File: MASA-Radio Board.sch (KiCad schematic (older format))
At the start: 35 parts, among them IC1 FAN4010IL6X_F113, IC2 FAN4010IL6X_F113, J1 SC_19-20, J2 Conn_01x03_Male, J3 Conn_01x02, J4 Conn_01x06, J5 Conn_01x06, J6 Conn_01x02, J7 UJ2-MBH-1-SMT-TR, U1 MP5077GG-Z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

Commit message: Modified CAN from 5.0V to 3.3V
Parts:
- renumbered R5 to R6, R6 to R7, R7 to R8, R8 to R9, U5 to U6
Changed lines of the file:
@@
 XBee
 $Sheet
-S 8050 6700 1150 2800
+S 8200 6700 1150 2800
 U 5E22EDDC
 F0 "CAN_Template" 50
 F1 "CAN_Template.sch" 50
-F2 "CAN_L" I L 8050 6850 50
-F3 "CAN_H" I L 8050 7050 50
-F4 "SI" I L 8050 7250 50
-F5 "SO" I L 8050 7450 50
-F6 "CS" I L 8050 7650 50
-F7 "SCK" I L 8050 7850 50
-F8 "INT" I L 8050 8100 50
-F9 "RX0BF" I L 8050 8300 50
-F10 "RX1BF" I L 8050 8500 50
-F11 "TX0RTS" I L 8050 8700 50
-F12 "TX1RTS" I L 8050 8950 50
-F13 "TX2RTS" I L 8050 9150 50
-F14 "RESET" I L 8050 9400 50
+F2 "CAN_L" I L 8200 6850 50
+F3 "CAN_H" I L 8200 7050 50
+F4 "SI" I L 8200 7250 50
+F5 "SO" I L 8200 7450 50
+F6 "CS" I L 8200 7650 50
+F7 "SCK" I L 8200 7850 50
+F8 "INT" I L 8200 8100 50
+F9 "RX0BF" I L 8200 8300 50
+F10 "RX1BF" I L 8200 8500 50
+F11 "TX0RTS" I L 8200 8700 50
+F12 "TX1RTS" I L 8200 8950 50
+F13 "TX2RTS" I L 8200 9150 50
+F14 "RESET" I L 8200 9400 50
 $EndSheet
-Text Notes 7850 10000 0    157  ~ 0
+Text Notes 7850 9950 0    157  ~ 0
 CAN_Template
-Text Notes 11450 5850 0    157  ~ 0
+Text Notes 11300 5850 0    157  ~ 0
 BL654PA MCU
 Wire Wire Line
@@
 	0    -1   -1   0
 $EndComp
-Text GLabel 8050 6850 0    50   Input ~ 0
+Text GLabel 8200 6850 0    50   Input ~ 0
 CAN_L
-Text GLabel 8050 7050 0    50   Input ~ 0
+Text GLabel 8200 7050 0    50   Input ~ 0
 CAN_H
-Text GLabel 8050 8100 0    50   Input ~ 0
+Text GLabel 8200 8100 0    50   Input ~ 0
 CAN_INT
-Text GLabel 8050 7650 0    50   Input ~ 0
+Text GLabel 8200 7650 0    50   Input ~ 0
 CS
-Text GLabel 8050 7850 0    50   Input ~ 0
+Text GLabel 8200 7850 0    50   Input ~ 0
 SPI_CLK
-Text GLabel 8050 9400 0    50   Input ~ 0
+Text GLabel 8200 9400 0    50   Input ~ 0
 CAN_RST
-Text GLabel 8050 9150 0    50   Input ~ 0
+Text GLabel 8200 9150 0    50   Input ~ 0
 TX2RTS
-Text GLabel 8050 8950 0    50   Input ~ 0
+Text GLabel 8200 8950 0    50   Input ~ 0
 TX1RTS
-Text GLabel 8050 8700 0    50   Input ~ 0
+Text GLabel 8200 8700 0    50   Input ~ 0
 TX0RTS
-Text GLabel 8050 8500 0    50   Input ~ 0
+Text GLabel 8200 8500 0    50   Input ~ 0
 RX1BF
-Text GLabel 8050 8300 0    50   Input ~ 0
+Text GLabel 8200 8300 0    50   Input ~ 0
 RX0BF
 Text GLabel 10450 3950 0    50   Input ~ 0
@@
 Text GLabel 10450 4050 0    50   Input ~ 0
 SPI_MOSI
-Text GLabel 8050 7450 0    50   Input ~ 0
+Text GLabel 8200 7450 0    50   Input ~ 0
 SPI_MISO
-Text GLabel 8050 7250 0    50   Input ~ 0
+Text GLabel 8200 7250 0    50   Input ~ 0
 SPI_MOSI
 Text GLabel 10450 4250 0    50   Input ~ 0
@@
 Current Sense IC
 $Comp
-L MASA_Library:MP5077GG-Z U5
+L MASA_Library:MP5077GG-Z U6
 U 1 1 5E25F7C2
 P 3700 11750
-F 0 "U5" H 3700 12165 50  0000 C CNN
+F 0 "U6" H 3700 12165 50  0000 C CNN
 F 1 "MP5077GG-Z" H 3700 12074 50  0000 C CNN
 F 2 "MASA_Library:MP5077GG-Z" H 3700 11650 50  0001 C CNN
@@
 $EndComp
 $Comp
-L Device:R_Small_US R5
+L Device:R_Small_US R6
 U 1 1 5E278AC5
 P 4350 12000
-F 0 "R5" V 4145 12000 50  0000 C CNN
+F 0 "R6" V 4145 12000 50  0000 C CNN
 F 1 "820k" V 4236 12000 50  0000 C CNN
 F 2 "" H 4350 12000 50  0001 C CNN
@@
 	5050 11900 5050 11950
 $Comp
-L Device:R_US R6
+L Device:R_US R7
 U 1 1 5E285E1D
 P 5350 11950
-F 0 "R6" V 5280 12068 50  0000 C CNN
+F 0 "R7" V 5280 12068 50  0000 C CNN
 F 1 "1" V 5267 11832 50  0000 C CNN
 F 2 "" V 5390 11940 50  0001 C CNN
@@
 Connection ~ 4700 11600
 $Comp
-L Device:R_Small_US R7
+L Device:R_Small_US R8
 U 1 1 5E28C88E
 P 6300 11950
-F 0 "R7" H 6368 11996 50  0000 L CNN
+F 0 "R8" H 6368 11996 50  0000 L CNN
 F 1 "1" H 6368 11905 50  0000 L CNN
 F 2 "" H 6300 11950 50  0001 C CNN
@@
 $EndComp
 $Comp
-L Device:R_Small_US R8
+L Device:R_Small_US R9
 U 1 1 5E298170
 P 6850 11950
-F 0 "R8" H 6918 11996 50  0000 L CNN
+F 0 "R9" H 6918 11996 50  0000 L CNN
 F 1 "3k" H 6918 11905 50  0000 L CNN
 F 2 "" H 6850 11950 50  0001 C CNN

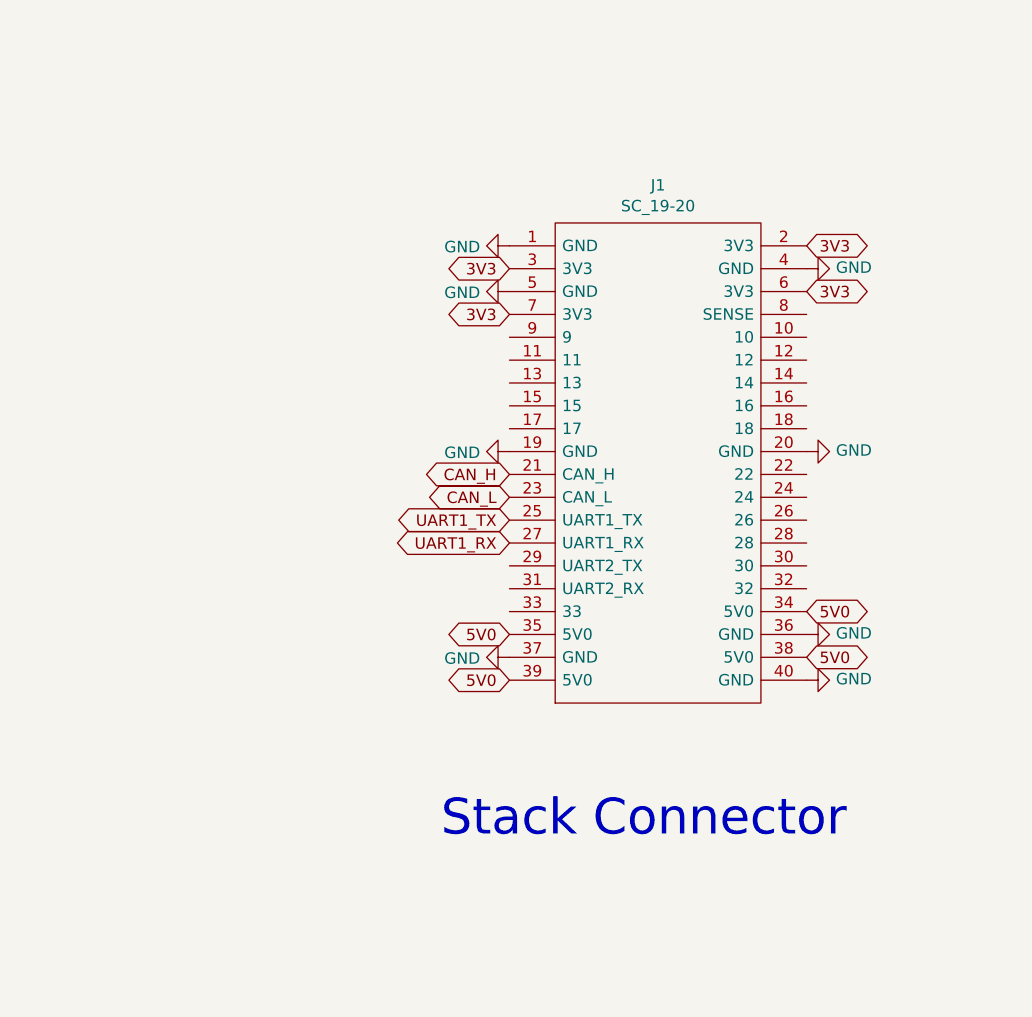
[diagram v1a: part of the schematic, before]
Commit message: Connected stack to xbee
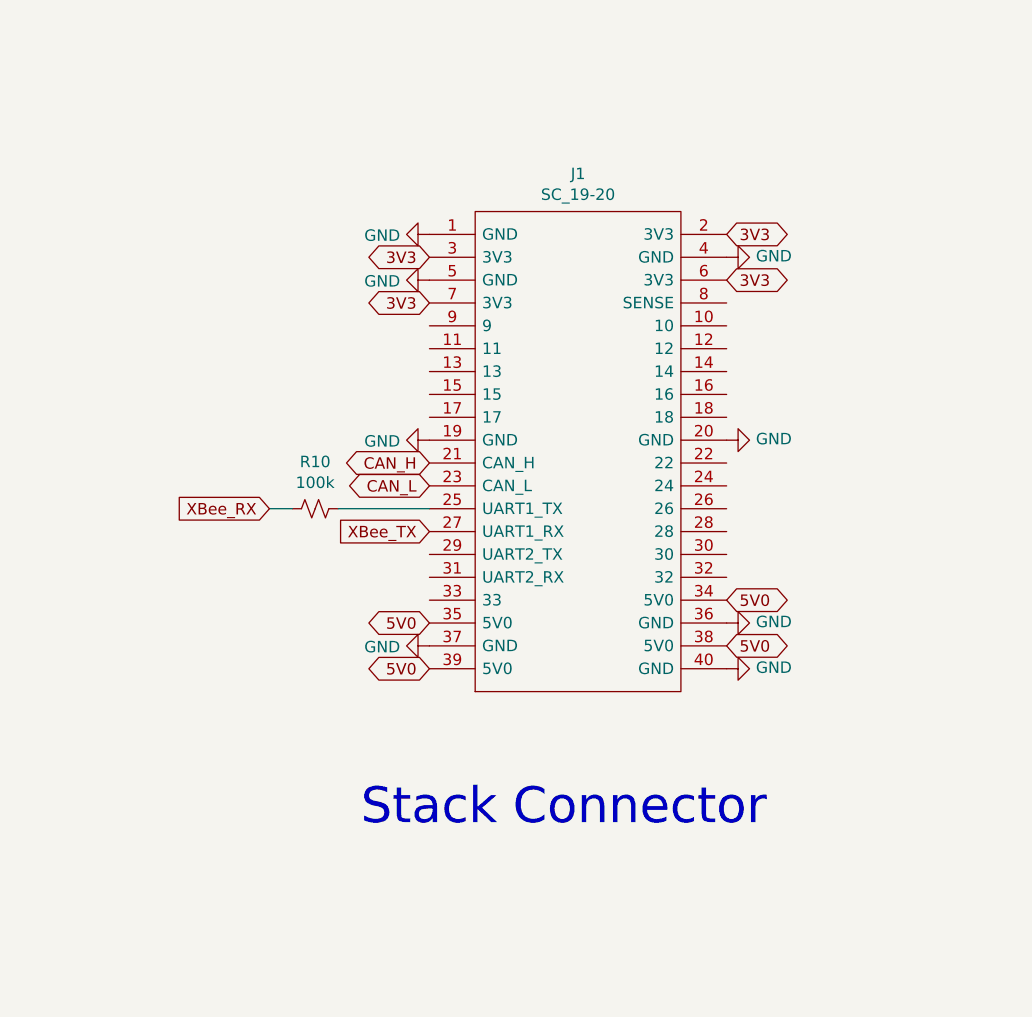
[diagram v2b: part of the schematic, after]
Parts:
- added R10: 100k, symbol Device:R_Small_US
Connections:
- net UART1_RX is gone; now on net XBee_TX: J1.27 (UART1_RX)
- net XBee_RX: now also R10.2
- net UART1_TX: no longer names the net of J1.25 (UART1_TX)
- net UART1_TX: now also R10.1
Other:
- moved on the sheet: J1
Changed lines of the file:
@@
 L MASA_Library:SC_19-20 J1
 U 1 1 5DFD7631
-P 12700 7300
-F 0 "J1" H 12700 7465 50  0000 C CNN
-F 1 "SC_19-20" H 12700 7374 50  0000 C CNN
-F 2 "MASA_Library:Stack_Connector_2019_2020" H 12450 7450 50  0001 L CNN
-F 3 "" H 12450 7950 50  0001 L CNN
-F 4 "Conn Shrouded Header HDR 40 POS 1.27mm Solder ST SMD T/R" H 12450 7850 50  0001 L CNN "Description"
-F 5 "11.35" H 12450 7650 50  0001 L CNN "Height"
-F 6 "SAMTEC" H 12450 7550 50  0001 L CNN "Manufacturer_Name"
-F 7 "TFC-120-32-F-D-A-K-TR" H 12450 7750 50  0001 L CNN "Manufacturer_Part_Number"
-	1    12700 7300
+P 12350 7250
+F 0 "J1" H 12350 7415 50  0000 C CNN
+F 1 "SC_19-20" H 12350 7324 50  0000 C CNN
+F 2 "MASA_Library:Stack_Connector_2019_2020" H 12100 7400 50  0001 L CNN
+F 3 "" H 12100 7900 50  0001 L CNN
+F 4 "Conn Shrouded Header HDR 40 POS 1.27mm Solder ST SMD T/R" H 12100 7800 50  0001 L CNN "Description"
+F 5 "11.35" H 12100 7600 50  0001 L CNN "Height"
+F 6 "SAMTEC" H 12100 7500 50  0001 L CNN "Manufacturer_Name"
+F 7 "TFC-120-32-F-D-A-K-TR" H 12100 7700 50  0001 L CNN "Manufacturer_Part_Number"
+	1    12350 7250
 	1    0    0    -1
 $EndComp
@@
 L power:GND #PWR01
 U 1 1 5DFDA903
-P 12050 7400
-F 0 "#PWR01" H 12050 7150 50  0001 C CNN
-F 1 "GND" V 12055 7272 50  0000 R CNN
-F 2 "" H 12050 7400 50  0001 C CNN
-F 3 "" H 12050 7400 50  0001 C CNN
-	1    12050 7400
+P 11700 7350
+F 0 "#PWR01" H 11700 7100 50  0001 C CNN
+F 1 "GND" V 11705 7222 50  0000 R CNN
+F 2 "" H 11700 7350 50  0001 C CNN
+F 3 "" H 11700 7350 50  0001 C CNN
+	1    11700 7350
 	0    1    1    0
 $EndComp
@@
 L power:GND #PWR02
 U 1 1 5DFDB255
-P 12050 7600
-F 0 "#PWR02" H 12050 7350 50  0001 C CNN
-F 1 "GND" V 12055 7472 50  0000 R CNN
-F 2 "" H 12050 7600 50  0001 C CNN
-F 3 "" H 12050 7600 50  0001 C CNN
-	1    12050 7600
+P 11700 7550
+F 0 "#PWR02" H 11700 7300 50  0001 C CNN
+F 1 "GND" V 11705 7422 50  0000 R CNN
+F 2 "" H 11700 7550 50  0001 C CNN
+F 3 "" H 11700 7550 50  0001 C CNN
+	1    11700 7550
 	0    1    1    0
 $EndComp
@@
 L power:GND #PWR05
 U 1 1 5DFDBEC5
-P 13350 7500
-F 0 "#PWR05" H 13350 7250 50  0001 C CNN
-F 1 "GND" V 13355 7372 50  0000 R CNN
-F 2 "" H 13350 7500 50  0001 C CNN
-F 3 "" H 13350 7500 50  0001 C CNN
-	1    13350 7500
+P 13000 7450
+F 0 "#PWR05" H 13000 7200 50  0001 C CNN
+F 1 "GND" V 13005 7322 50  0000 R CNN
+F 2 "" H 13000 7450 50  0001 C CNN
+F 3 "" H 13000 7450 50  0001 C CNN
+	1    13000 7450
 	0    -1   -1   0
 $EndComp
@@
 L power:GND #PWR06
 U 1 1 5DFDC70F
-P 13350 8300
-F 0 "#PWR06" H 13350 8050 50  0001 C CNN
-F 1 "GND" V 13355 8172 50  0000 R CNN
-F 2 "" H 13350 8300 50  0001 C CNN
-F 3 "" H 13350 8300 50  0001 C CNN
-	1    13350 8300
+P 13000 8250
+F 0 "#PWR06" H 13000 8000 50  0001 C CNN
+F 1 "GND" V 13005 8122 50  0000 R CNN
+F 2 "" H 13000 8250 50  0001 C CNN
+F 3 "" H 13000 8250 50  0001 C CNN
+	1    13000 8250
 	0    -1   -1   0
 $EndComp
@@
 L power:GND #PWR03
 U 1 1 5DFDD019
-P 12050 8300
-F 0 "#PWR03" H 12050 8050 50  0001 C CNN
-F 1 "GND" V 12055 8172 50  0000 R CNN
-F 2 "" H 12050 8300 50  0001 C CNN
-F 3 "" H 12050 8300 50  0001 C CNN
-	1    12050 8300
+P 11700 8250
+F 0 "#PWR03" H 11700 8000 50  0001 C CNN
+F 1 "GND" V 11705 8122 50  0000 R CNN
+F 2 "" H 11700 8250 50  0001 C CNN
+F 3 "" H 11700 8250 50  0001 C CNN
+	1    11700 8250
 	0    1    1    0
 $EndComp
@@
 L power:GND #PWR07
 U 1 1 5DFDD67F
-P 13350 9100
-F 0 "#PWR07" H 13350 8850 50  0001 C CNN
-F 1 "GND" V 13355 8972 50  0000 R CNN
-F 2 "" H 13350 9100 50  0001 C CNN
-F 3 "" H 13350 9100 50  0001 C CNN
-	1    13350 9100
+P 13000 9050
+F 0 "#PWR07" H 13000 8800 50  0001 C CNN
+F 1 "GND" V 13005 8922 50  0000 R CNN
+F 2 "" H 13000 9050 50  0001 C CNN
+F 3 "" H 13000 9050 50  0001 C CNN
+	1    13000 9050
 	0    -1   -1   0
 $EndComp
@@
 L power:GND #PWR08
 U 1 1 5DFDDD0D
-P 13350 9300
-F 0 "#PWR08" H 13350 9050 50  0001 C CNN
-F 1 "GND" V 13355 9172 50  0000 R CNN
-F 2 "" H 13350 9300 50  0001 C CNN
-F 3 "" H 13350 9300 50  0001 C CNN
-	1    13350 9300
+P 13000 9250
+F 0 "#PWR08" H 13000 9000 50  0001 C CNN
+F 1 "GND" V 13005 9122 50  0000 R CNN
+F 2 "" H 13000 9250 50  0001 C CNN
+F 3 "" H 13000 9250 50  0001 C CNN
+	1    13000 9250
 	0    -1   -1   0
 $EndComp
@@
 L power:GND #PWR04
 U 1 1 5DFDDF0B
-P 12050 9200
-F 0 "#PWR04" H 12050 8950 50  0001 C CNN
-F 1 "GND" V 12055 9072 50  0000 R CNN
-F 2 "" H 12050 9200 50  0001 C CNN
-F 3 "" H 12050 9200 50  0001 C CNN
-	1    12050 9200
-	0    1    1    0
-$EndComp
-Text GLabel 12050 7500 0    50   BiDi ~ 0
+P 11700 9150
+F 0 "#PWR04" H 11700 8900 50  0001 C CNN
+F 1 "GND" V 11705 9022 50  0000 R CNN
+F 2 "" H 11700 9150 50  0001 C CNN
+F 3 "" H 11700 9150 50  0001 C CNN
+	1    11700 9150
+	0    1    1    0
+$EndComp
+Text GLabel 11700 7450 0    50   BiDi ~ 0
 3V3
-Text GLabel 12050 7700 0    50   BiDi ~ 0
+Text GLabel 11700 7650 0    50   BiDi ~ 0
 3V3
-Text GLabel 13350 7400 2    50   BiDi ~ 0
+Text GLabel 13000 7350 2    50   BiDi ~ 0
 3V3
-Text GLabel 13350 7600 2    50   BiDi ~ 0
+Text GLabel 13000 7550 2    50   BiDi ~ 0
 3V3
-Text GLabel 12050 9100 0    50   BiDi ~ 0
-5V0
-Text GLabel 12050 9300 0    50   BiDi ~ 0
-5V0
-Text GLabel 13350 9200 2    50   BiDi ~ 0
-5V0
-Text GLabel 13350 9000 2    50   BiDi ~ 0
-5V0
-Text GLabel 12050 8400 0    50   BiDi ~ 0
+Text GLabel 11700 9050 0    50   BiDi ~ 0
+5V0
+Text GLabel 11700 9250 0    50   BiDi ~ 0
+5V0
+Text GLabel 13000 9150 2    50   BiDi ~ 0
+5V0
+Text GLabel 13000 8950 2    50   BiDi ~ 0
+5V0
+Text GLabel 11700 8350 0    50   BiDi ~ 0
 CAN_H
-Text GLabel 12050 8500 0    50   BiDi ~ 0
+Text GLabel 11700 8450 0    50   BiDi ~ 0
 CAN_L
-Text GLabel 12050 8600 0    50   BiDi ~ 0
-UART1_TX
-Text GLabel 12050 8700 0    50   BiDi ~ 0
-UART1_RX
-Text Notes 11750 10000 0    157  ~ 0
+Text Notes 11400 9950 0    157  ~ 0
 Stack Connector
 $Comp
@@
 	0    1    1    0
 $EndComp
+Text GLabel 11000 8550 0    50   Input ~ 0
+XBee_RX
+Text GLabel 11700 8650 0    50   Input ~ 0
+XBee_TX
+$Comp
+L Device:R_Small_US R10
+U 1 1 5E2D0F89
+P 11200 8550
+F 0 "R10" V 10995 8550 50  0000 C CNN
+F 1 "100k" V 11086 8550 50  0000 C CNN
+F 2 "" H 11200 8550 50  0001 C CNN
+F 3 "~" H 11200 8550 50  0001 C CNN
+	1    11200 8550
+	0    1    1    0
+$EndComp
+Wire Wire Line
+	11000 8550 11100 8550
+Wire Wire Line
+	11700 8550 11300 8550
 $EndSCHEMATC
